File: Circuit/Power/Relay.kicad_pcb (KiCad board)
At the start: 2 copper layers, 33 x 20.3 mm, 14 parts, among them J1 Input, J2 Output, Q1 RFP30N06LE, Q2 RFP30N06LE, U2 PC817

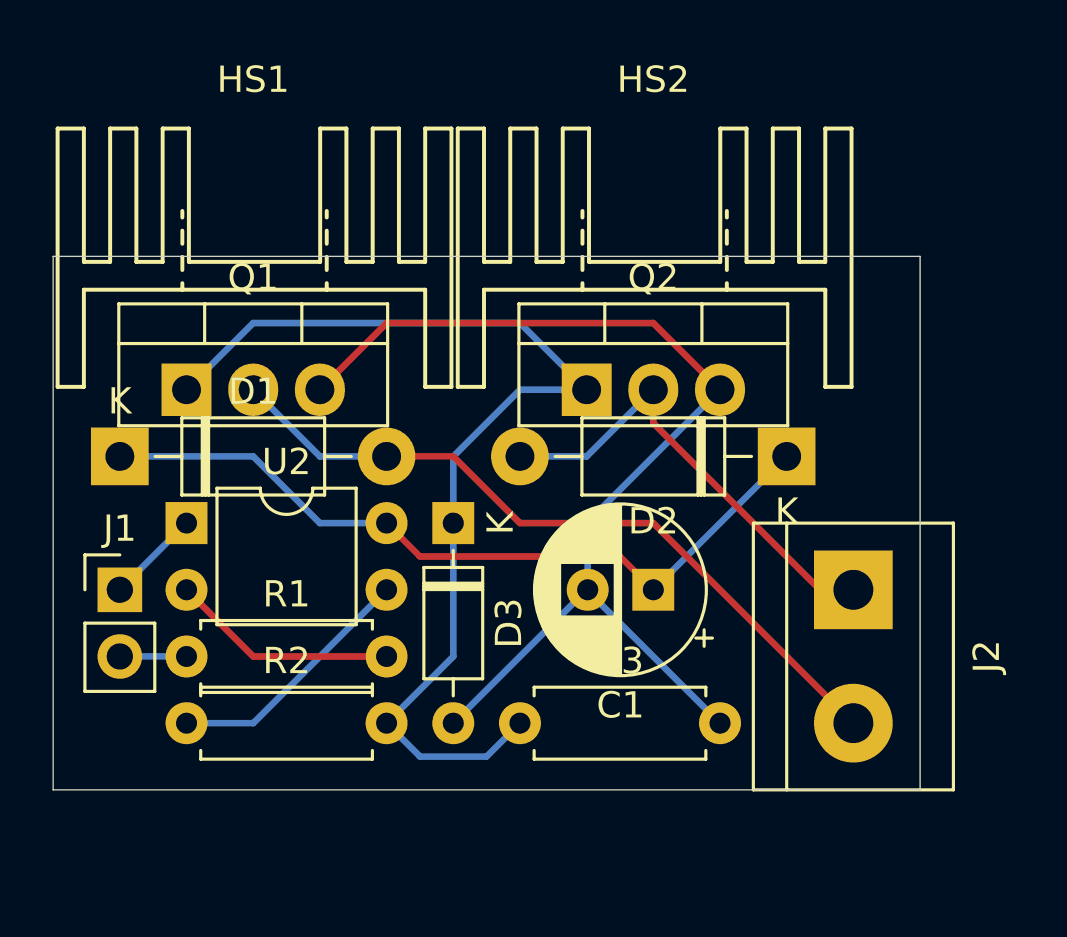
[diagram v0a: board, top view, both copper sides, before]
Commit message: [Circuit] Add switch adapter circuit
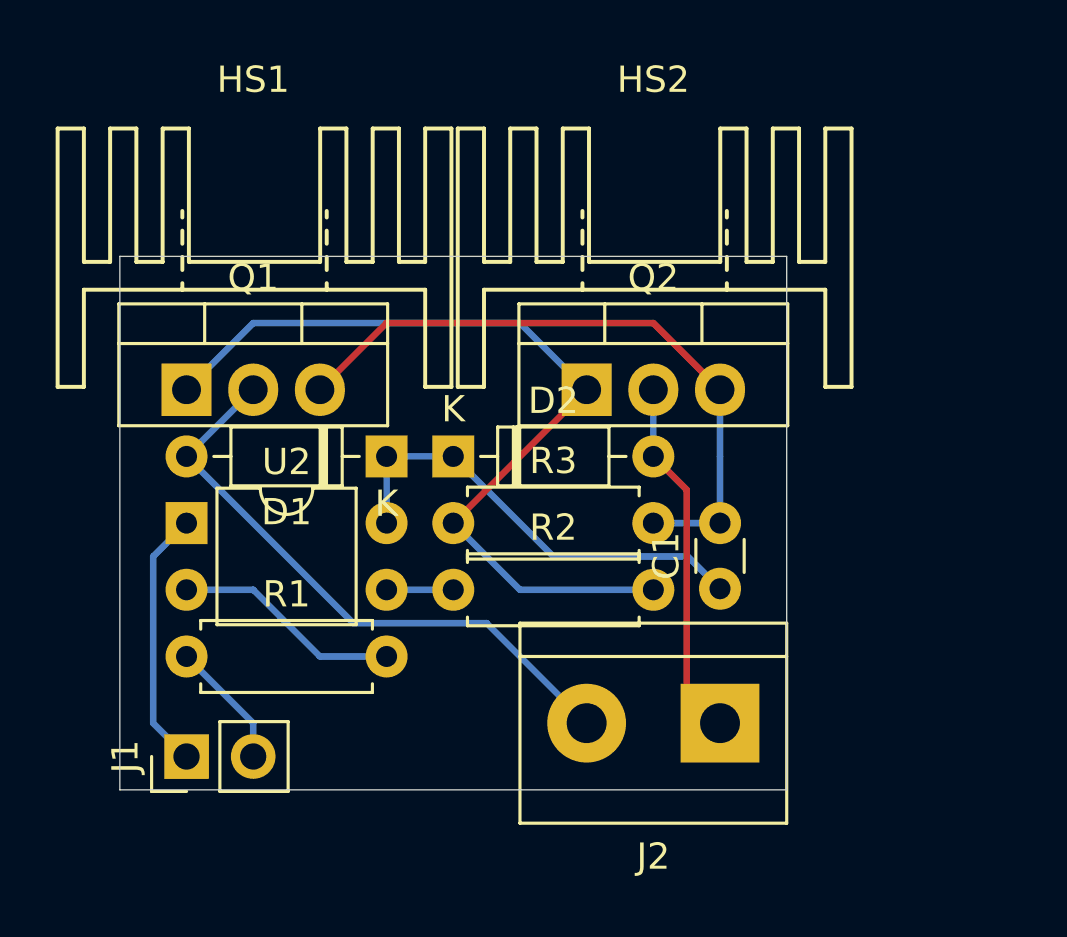
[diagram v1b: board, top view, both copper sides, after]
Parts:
- removed D3: 1N5242B, Diode_THT:D_DO-35_SOD27_P7.62mm_Horizontal
- C1: value 100uF -> 0.1uF; footprint Capacitor_THT:CP_Radial_D6.3mm_P2.50mm -> Capacitor_THT:C_Disc_D3.0mm_W1.6mm_P2.50mm
- D1, D2: value 1N4007 -> 1N4148; footprint Diode_THT:D_DO-41_SOD81_P10.16mm_Horizontal -> Diode_THT:D_DO-35_SOD27_P7.62mm_Horizontal
- moved D2 12.7 mm to (73.7, 50.8), turned to 0 degrees
- moved R2 11.4 mm to (73.7, 55.9)
- moved D1 10.2 mm to (71.1, 50.8), turned to 180 degrees
- moved R3 8.03 mm to (73.7, 53.3)
- moved J2 7.18 mm to (83.8, 61.0), turned to 180 degrees
- moved J1 6.84 mm to (63.5, 62.2), turned to 90 degrees
- moved C1 2.54 mm to (83.8, 55.8), turned to 90 degrees
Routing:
- net Net-(C1-Pad2): track 41.5 -> 25.0 mm
- net Net-(C1-Pad1): track 29.6 -> 17.4 mm
- net Net-(Q1-Pad1): track 40.8 -> 33.2 mm
- net Net-(R2-Pad1): track 9.72 -> 2.54 mm
- net /Input+: track 3.59 -> 9.94 mm
- net /Output1: track 28.1 -> 23.0 mm
- net /Output2: track 16.4 -> 13.8 mm
- net /Input-: track 2.54 -> 4.86 mm
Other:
- board size 33 x 20.3 mm -> 25.4 x 20.3 mm
